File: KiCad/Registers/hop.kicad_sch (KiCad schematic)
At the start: 38 parts, among them U16 74HC574, U17 74HC574, U18 74HC574, U19 74HC74, U20 74HCT157, U21 74HCT157, U22 74HCT157, U23 74HCT157, U24 74HCT157, U25 74HCT157, U26 74HCT157, U27 74HC86, U28 74HC86, U29 74HC08, U30 74HC08, U31 74HC74, U32 74HCT32, U33 74HC574, U34 74HC574, U35 74HC574, U36 74HC574, U41 74HCT157, U42 74HCT157, U43 74HCT157, U44 74HCT157, U45 74HCT157

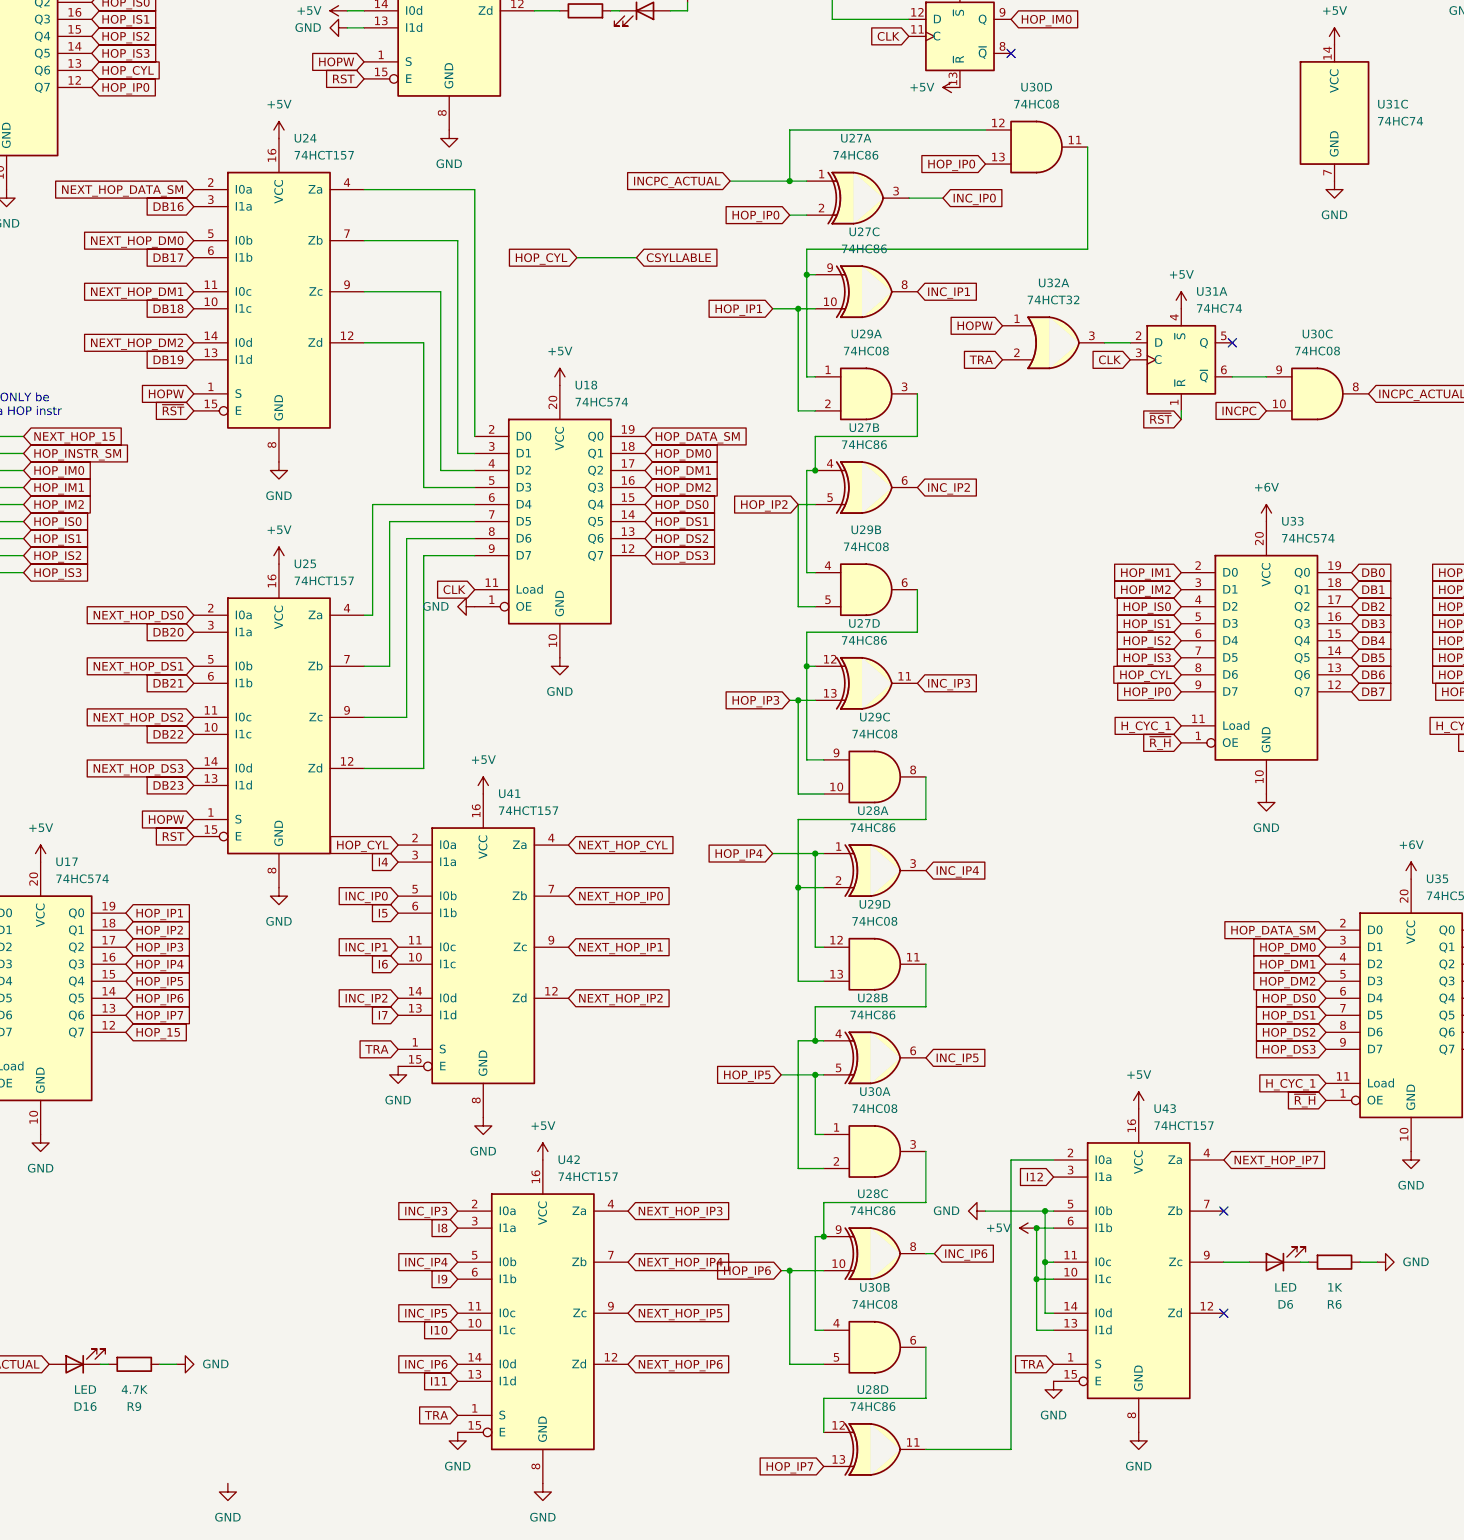
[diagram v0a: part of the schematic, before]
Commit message: Simple bootloader program.
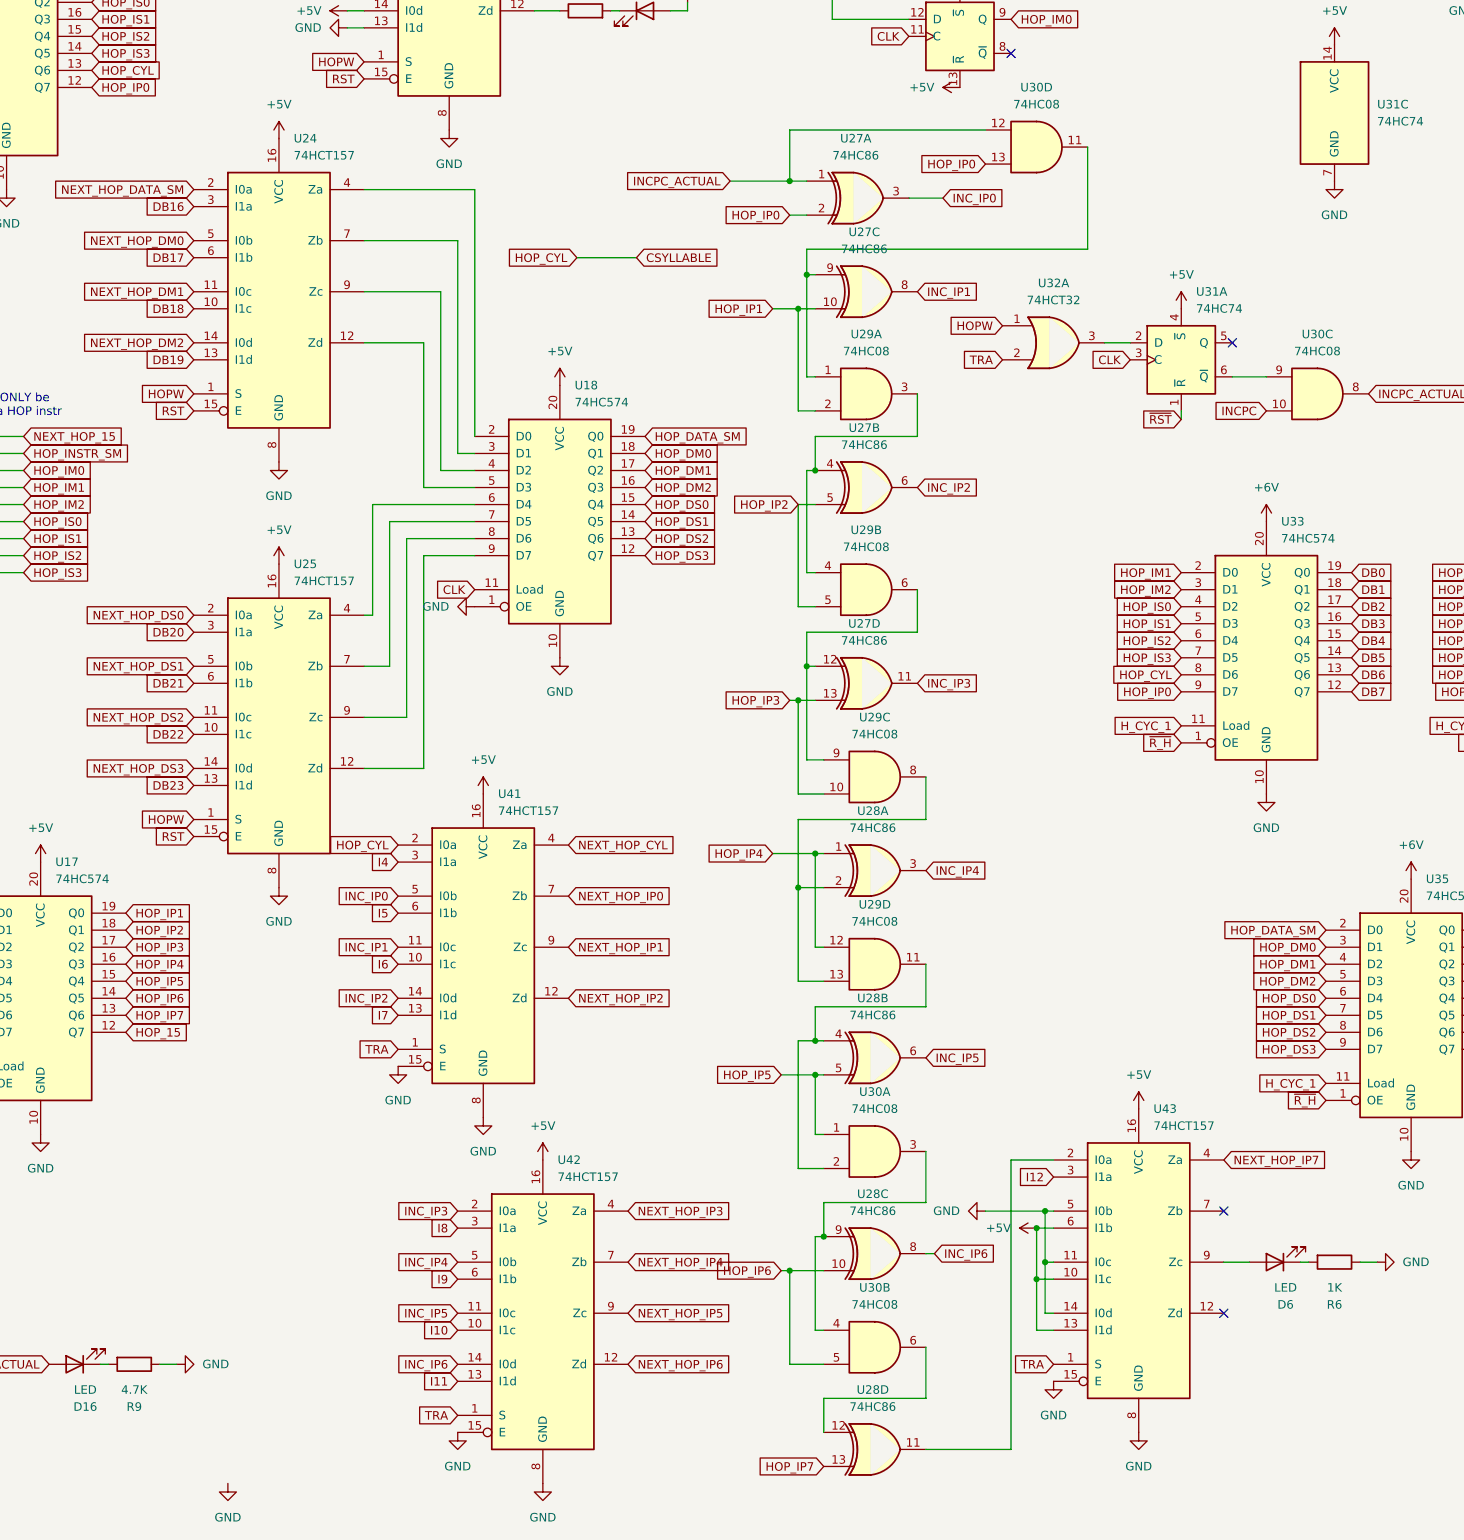
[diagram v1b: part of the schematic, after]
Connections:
- net RST: now also U24.15 (E)
- net ~{RST}: no longer U24.15 (E)
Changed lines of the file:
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@@
 (kicad_sch
-	(version 20231120)
+	(version 20250114)
 	(generator "eeschema")
-	(generator_version "8.0")
+	(generator_version "9.0")
 	(paper "A3")
+	(text "These can ONLY be\nchanged by a HOP instr"
+		(exclude_from_sim no)
+		(at 85.598 119.888 0)
+		(effects
+			(font
+				(size 1.27 1.27)
+			)
+		)
+	)
 	(junction
 		(at 241.3 242.57)
@@
 		)
 	)
-	(text "These can ONLY be\nchanged by a HOP instr"
-		(exclude_from_sim no)
-		(at 85.598 119.888 0)
-		(effects
-			(font
-				(size 1.27 1.27)
-			)
-		)
-	)
 	(global_label "HOP_DS3"
 		(shape input)
@@
 		)
 	)
+	(global_label "RST"
+		(shape input)
+		(at 115.57 120.65 180)
+		(fields_autoplaced yes)
+		(effects
+			(font
+				(size 1.27 1.27)
+			)
+			(justify right)
+		)
+		(property "Intersheetrefs" "${INTERSHEET_REFS}"
+			(at 109.1377 120.65 0)
+			(effects
+				(font
+					(size 1.27 1.27)
+				)
+				(justify right)
+				(hide yes)
+			)
+		)
+	)
 	(global_label "HOPW"
 		(shape input)
@@
 			(effects
 				(font
-					(size 1.27 1.27)
-				)
-				(justify right)
-				(hide yes)
-			)
-		)
-	)
-	(global_label "~{RST}"
-		(shape input)
-		(at 115.57 120.65 180)
-		(fields_autoplaced yes)
-		(effects
-			(font
-				(size 1.27 1.27)
-			)
-			(justify right)
-		)
-		(property "Intersheetrefs" "${INTERSHEET_REFS}"
-			(at 109.1377 120.65 0)
-			(effects
-				(font

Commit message: Update schematics with fixes.
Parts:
- added U51: 74HCT32, Package_SO:SO-14_3.9x8.65mm_P1.27mm, symbol 74xx:74LS32
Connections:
- net +5V: now also U51.14 (VCC)
- net GND: now also U51.1, U51.10, U51.2, U51.4, U51.5, U51.7 (GND), U51.9
- net HOPW: now also U51.12
- net TRA: now also U51.13
- net H_CYC_1 renamed HOP_COPY
- net HOP_COPY: now also U51.11
- no-connect marks 11 -> 13
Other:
- moved on the sheet: D16, R9
